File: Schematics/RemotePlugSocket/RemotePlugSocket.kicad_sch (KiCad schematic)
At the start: 12 parts, among them J1 BME280, J2 Relay_Module, J3 LED_Status, J4 1-Wire CH1, J5 Power, J6 Button, U1 ESP32-DevKitC

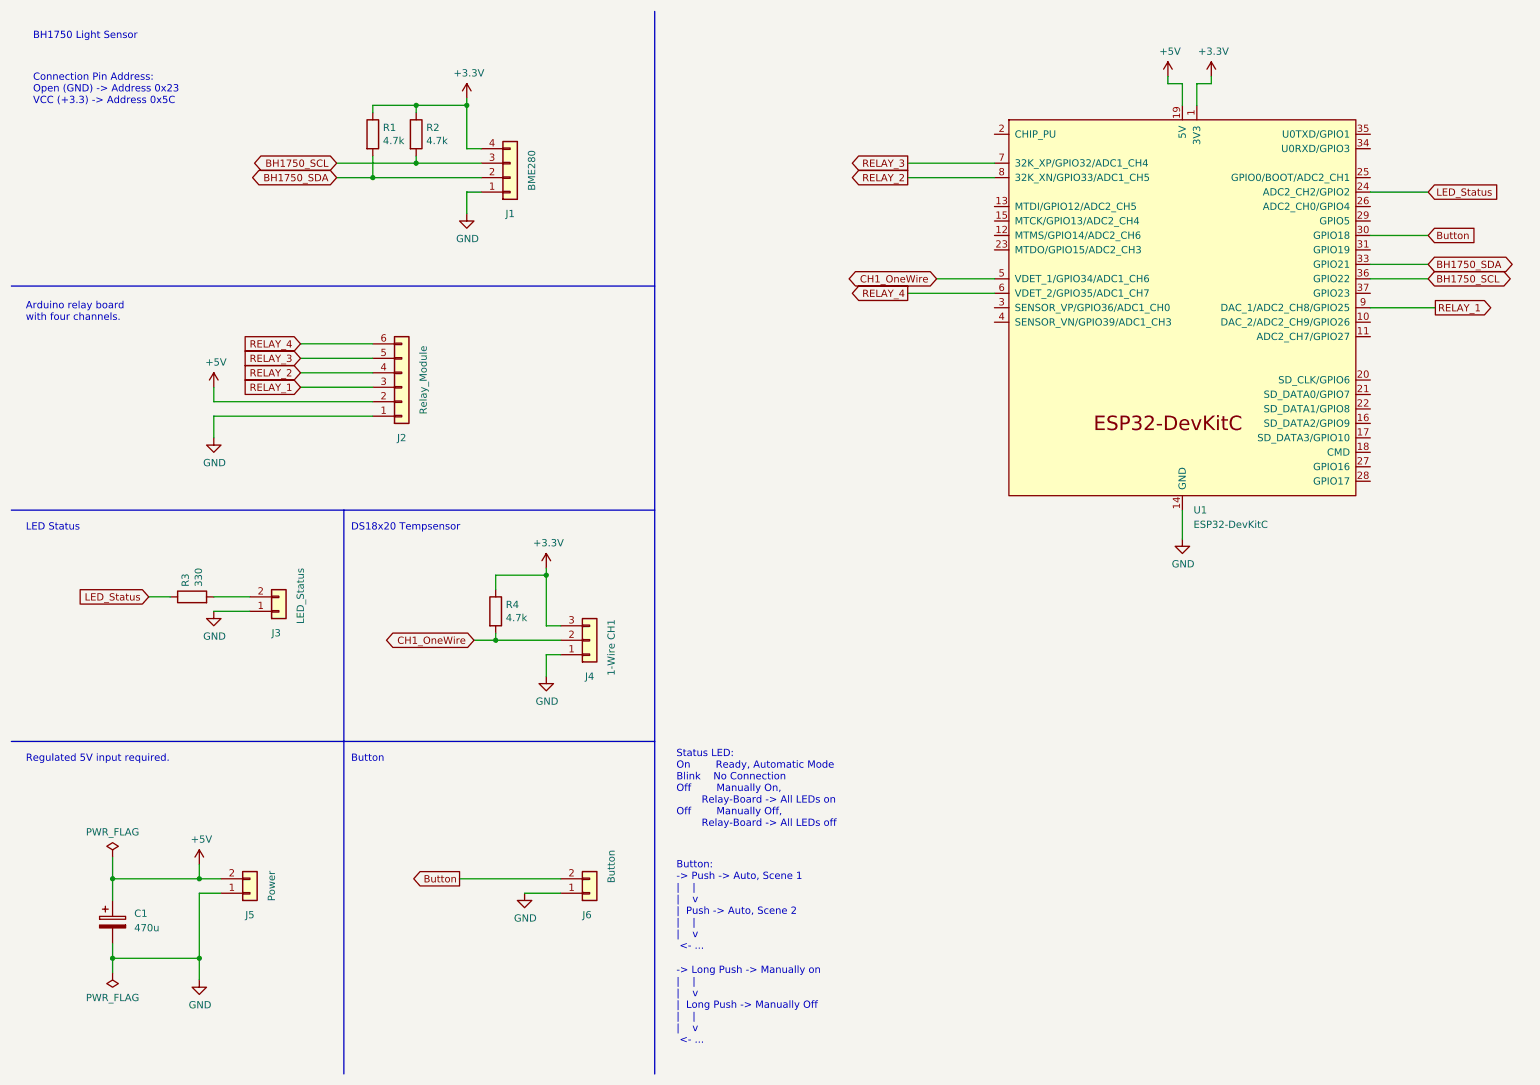
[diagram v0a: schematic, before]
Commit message: Schematics: pinning of relays and oneWire changed. StateMachine added.
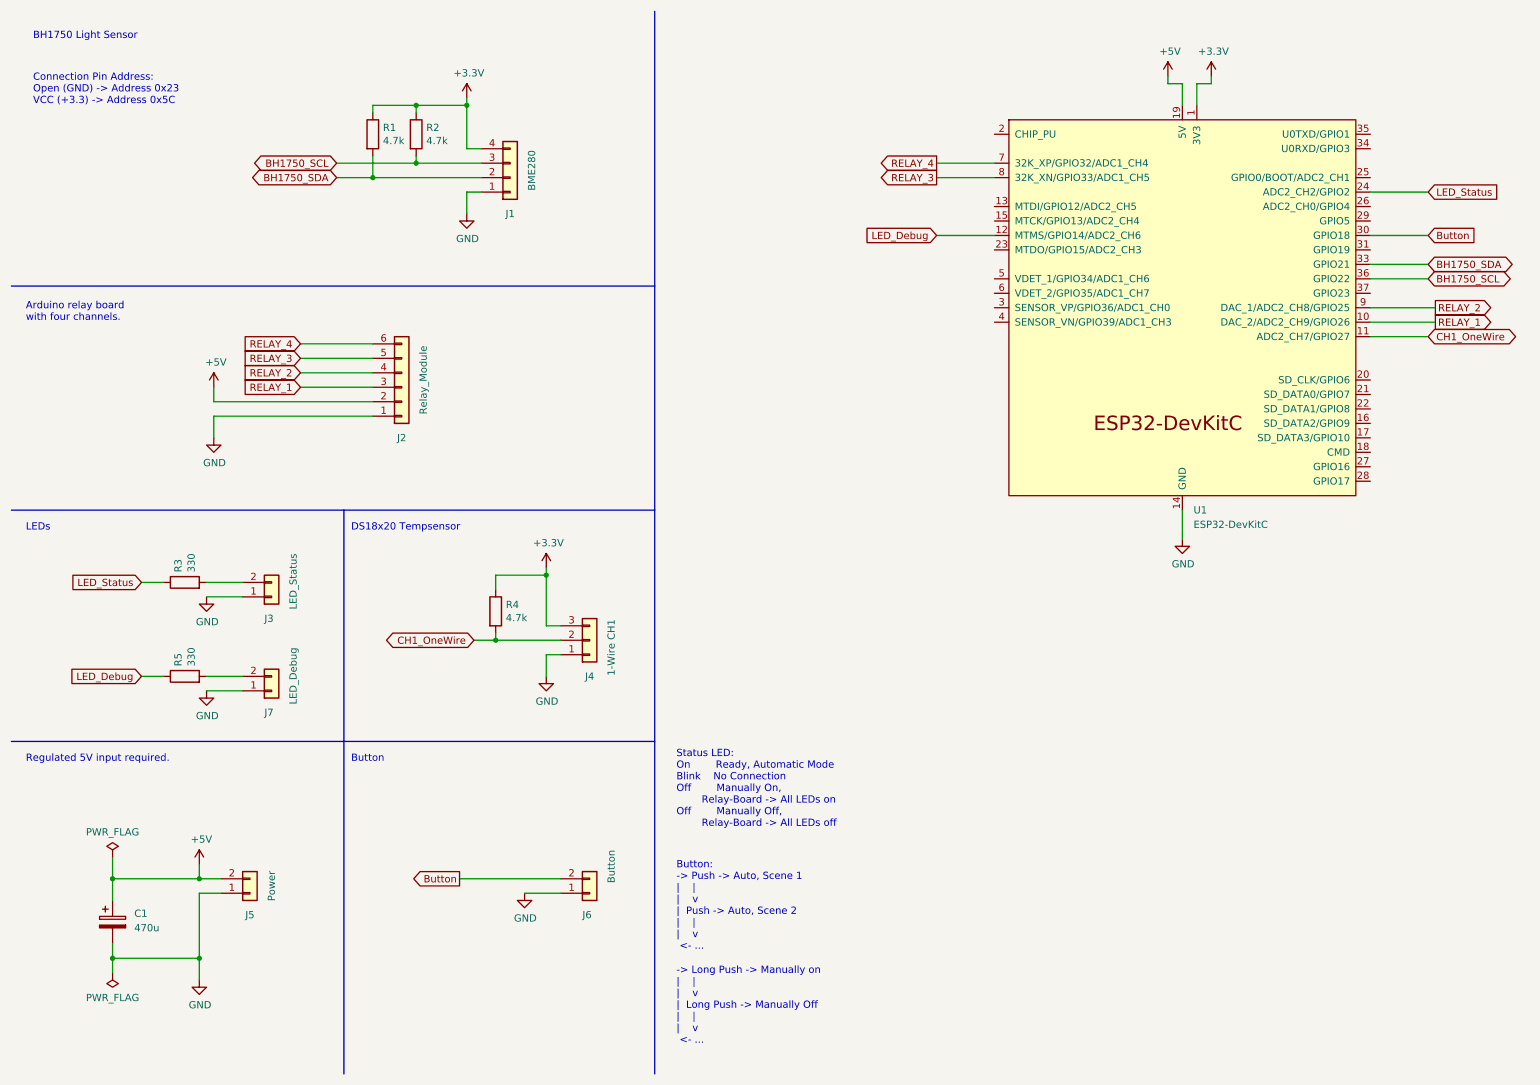
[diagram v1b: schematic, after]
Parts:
- added J7: LED_Debug, Connector_Molex:Molex_KK-254_AE-6410-02A_1x02_P2.54mm_Vertical, symbol Connector_Generic:Conn_01x02
- added R5: 330, Resistor_THT:R_Axial_DIN0207_L6.3mm_D2.5mm_P7.62mm_Horizontal, symbol Device:R
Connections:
- net CH1_OneWire: now also U1.11 (ADC2_CH7/GPIO27); no longer U1.5 (VDET_1/GPIO34/ADC1_CH6)
- net GND: now also J7.1 (Pin_1)
- net RELAY_1: now also U1.10 (DAC_2/ADC2_CH9/GPIO26); no longer U1.9 (DAC_1/ADC2_CH8/GPIO25)
- net RELAY_2: now also U1.9 (DAC_1/ADC2_CH8/GPIO25); no longer U1.8 (32K_XN/GPIO33/ADC1_CH5)
- net RELAY_3: now also U1.8 (32K_XN/GPIO33/ADC1_CH5); no longer U1.7 (32K_XP/GPIO32/ADC1_CH4)
- net RELAY_4: now also U1.7 (32K_XP/GPIO32/ADC1_CH4); no longer U1.6 (VDET_2/GPIO35/ADC1_CH7)
- net LED_Debug: now reaches U1.12 (MTMS/GPIO14/ADC2_CH6)
- net LED_Debug: now also R5.1
- new net: J7.2 (Pin_2), R5.2
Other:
- note added: "LEDs"
- note removed: "LED Status"
- moved on the sheet: J3, R3

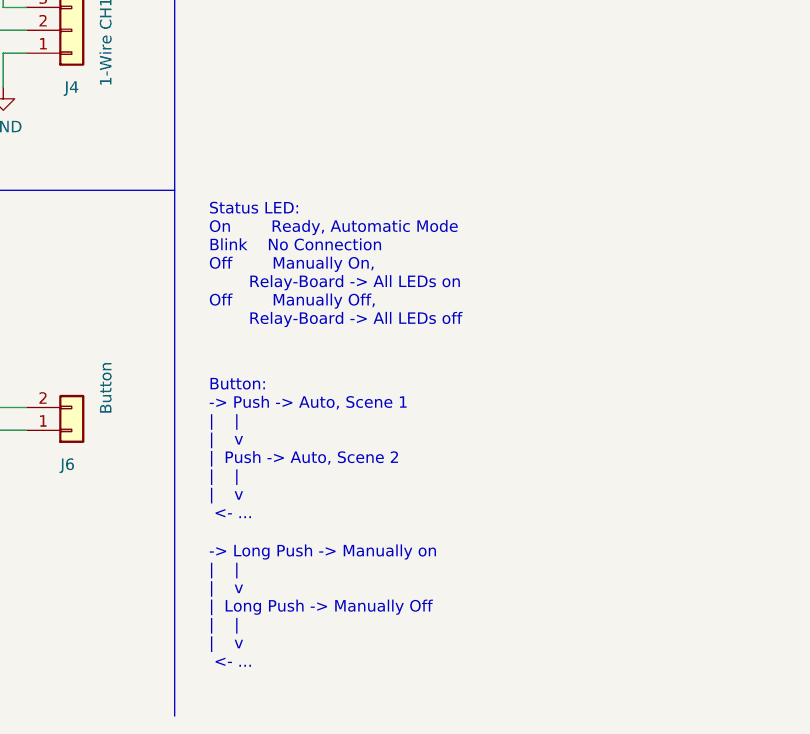
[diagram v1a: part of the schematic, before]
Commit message: Relay switching from HA now works.
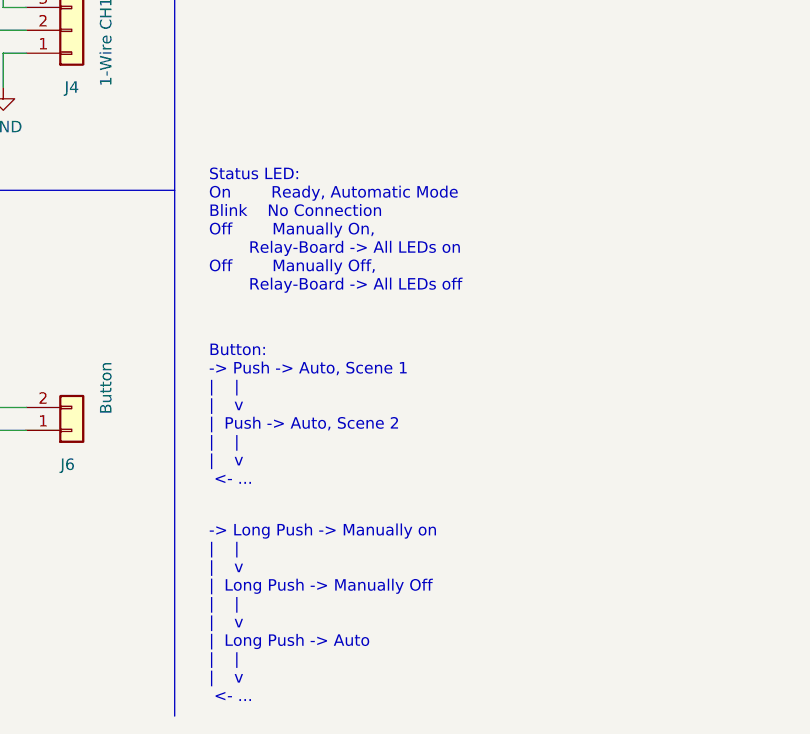
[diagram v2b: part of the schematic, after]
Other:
- note added: "-> Long Push -> Manually on | | | v | Long Push -> Manually Off | | | v | Long Push -> Auto | | | v <- ..."
- note removed: "-> Long Push -> Manually on | | | v | Long Push -> Manually Off | | | v <- ..."
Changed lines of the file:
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@@
   )
   (text "Status LED:\nOn		Ready, Automatic Mode\nBlink	No Connection\nOff		Manually On, \n		Relay-Board -> All LEDs on\nOff		Manually Off, \n		Relay-Board -> All LEDs off\n"
-    (at 128.27 154.94 0)
+    (at 128.27 151.13 0)
     (effects (font (size 1.27 1.27)) (justify left bottom))
   )
@@
     (effects (font (size 1.27 1.27)) (justify left bottom))
   )
-  (text "-> Long Push -> Manually on\n|    |\n|    v\n|  Long Push -> Manually Off\n|    |\n|    v\n <- ..."
-    (at 128.27 193.04 0)
+  (text "-> Long Push -> Manually on\n|    |\n|    v\n|  Long Push -> Manually Off\n|    |\n|    v\n|  Long Push -> Auto\n|    |\n|    v\n <- ..."
+    (at 128.27 196.85 0)
     (effects (font (size 1.27 1.27)) (justify left bottom))
   )
@@
   )
   (text "Button:\n-> Push -> Auto, Scene 1\n|    |\n|    v\n|  Push -> Auto, Scene 2\n|    |\n|    v\n <- ..."
-    (at 128.27 176.53 0)
+    (at 128.27 172.72 0)
     (effects (font (size 1.27 1.27)) (justify left bottom))
   )
